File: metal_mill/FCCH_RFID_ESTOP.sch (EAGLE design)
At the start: 31 parts, among them Q1 BC846ALT1SMD, Q2 BC846ALT1SMD, Q3 2N3906, Q4 2N3906, Q5 2N3906

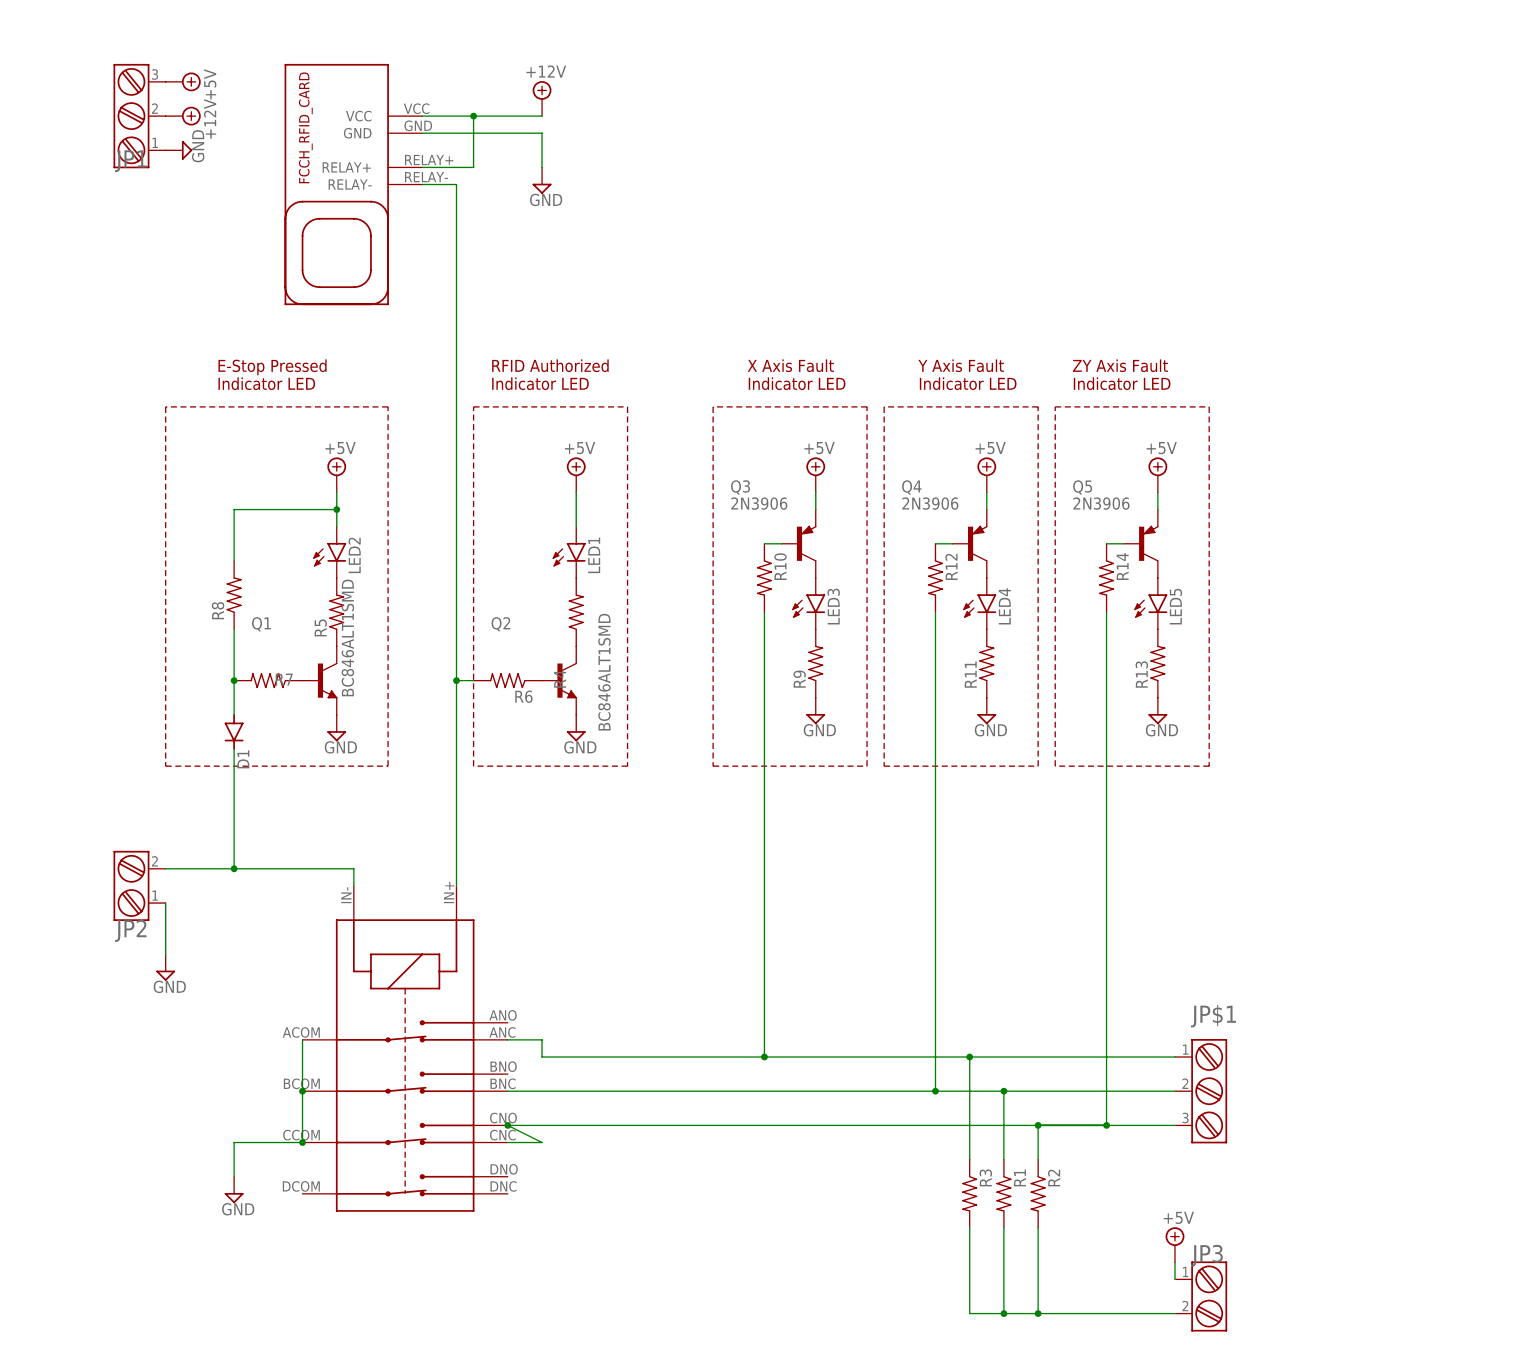
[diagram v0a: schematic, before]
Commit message: Added FCCH_RFID_ESTOP board layout and wire harnesses description in README.md
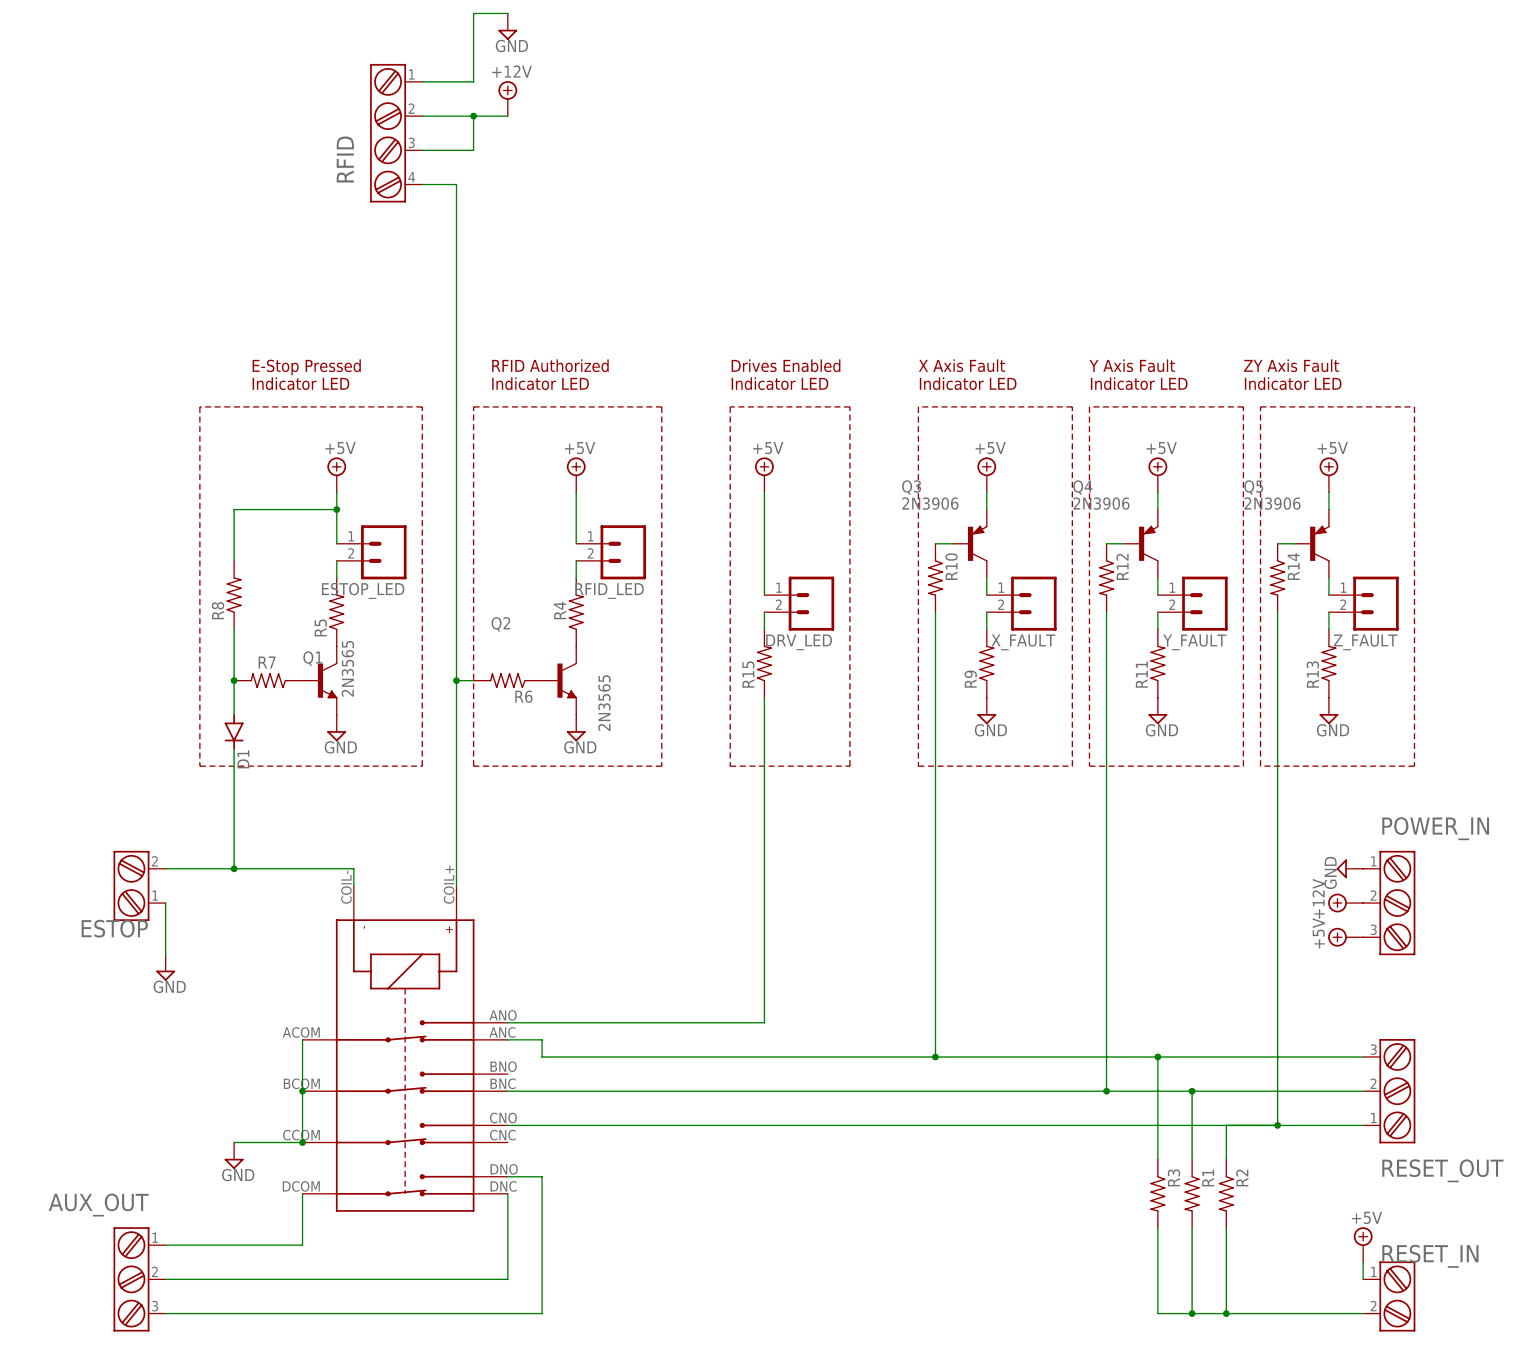
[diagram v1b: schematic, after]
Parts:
- removed JP$1, JP1: EURO-CON-3_2.54P, zahaComponents:EURO-CON-3_2.54P
- removed JP2, JP3: EURO-CON-2_2.54P, zahaComponents:EURO-CON-2_2.54P
- removed LED1, LED2, LED3, LED4, LED5: (no value), led:LED3MM
- removed U$2: RELAY_4PDT, fcch_eagle_parts_metal_mill:RELAY_4PDT
- removed U$3: FCCH_RFID_CARD, fcch_eagle_parts_metal_mill:FCCH_RFID_CARD
- added AUX_OUT, POWER_IN, RESET_OUT: EURO-CON-3_2.54P, fcch_eagle_parts_metal_mill:EURO-CON-3_2.54P
- added DRV_LED, ESTOP_LED, RFID_LED, X_FAULT, Y_FAULT, Z_FAULT: (no value), con-amp-quick:M02
- added ESTOP, RESET_IN: EURO-CON-2_2.54P, fcch_eagle_parts_metal_mill:EURO-CON-2_2.54P
- added R15: (no value), rcl:R-US_0204/7
- added RFID: EURO-CON-4_2.54P, fcch_eagle_parts_metal_mill:EURO-CON-4_2.54P
- added U$1: NC4D-JP-DC5V, fcch_eagle_parts_metal_mill:NC4D-JP-DC5V
- Q1, Q2: value BC846ALT1SMD -> 2N3565; device transistor-npn:BC846ALT1SMD -> transistor-npn:2N3565
- R1, R10, R11, R12, R13, R14, R2, R3, R4, R5, R6, R7, R8, R9: device rcl:R-US_M0805 -> rcl:R-US_0204/7
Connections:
- removed net N$1: JP$1.1, R10.2, R3.1, U$2.ANC
- removed net N$12: LED2.C, R5.2
- removed net N$13: D1.C, JP2.2, U$2.P$2
- removed net N$14: LED3.A, Q3.C
- removed net N$2: JP$1.2, R1.1, R12.2, U$2.BNC
- removed net N$3: JP$1.3, R14.2, R2.1, U$2.CNC, U$2.CNO
- removed net N$4: LED1.C, R4.2
- removed net N$6: R6.2, U$2.P$1, U$3.RELAY-
- new net ANO: R15.1, U$1.ANO
- new net AUX_RELAY_COM: AUX_OUT.1, U$1.DCOM
- new net AUX_RELAY_NC: AUX_OUT.2, U$1.DNC
- new net AUX_RELAY_NO: AUX_OUT.3, U$1.DNO
- new net ESTOP: D1.C, ESTOP.2, U$1.COIL-
- new net N$21: R9.2, X_FAULT.2
- new net N$25: R11.2, Y_FAULT.2
- new net N$26: Q5.C, Z_FAULT.1
- new net N$27: R13.2, Z_FAULT.2
- new net RFID_ENABLE: R6.2, RFID.4, U$1.COIL+
- new net X_ERR/RES: R10.2, R3.1, RESET_OUT.3, U$1.ANC
- new net Y_ERR/RES: R1.1, R12.2, RESET_OUT.2, U$1.BNC
- new net Z_ERR/RES: R14.2, R2.1, RESET_OUT.1, U$1.CNO
- net +12V: now also POWER_IN.2, RFID.2, RFID.3; no longer JP1.2, U$3.RELAY+, U$3.VCC
- net +5V: now also DRV_LED.1, ESTOP_LED.1, POWER_IN.3, RESET_IN.1, RFID_LED.1; no longer JP1.3, JP3.1, LED1.A, LED2.A
- net GND: now also ESTOP.1, POWER_IN.1, RFID.1, U$1.ACOM, U$1.BCOM, U$1.CCOM; no longer JP1.1, JP2.1, U$2.ACOM, U$2.BCOM, U$2.CCOM, U$3.GND
- net N$15: now also ESTOP_LED.2, R5.2; no longer LED3.C, R9.2
- net N$17: now also R4.2, RFID_LED.2; no longer LED4.A, Q4.C
- net N$18: now also DRV_LED.2, R15.2; no longer LED5.A, Q5.C
- net N$19: now also Q3.C, X_FAULT.1; no longer LED4.C, R11.2
- net N$23: now also Q4.C, Y_FAULT.1; no longer LED5.C, R13.2
- net N$7: now also RESET_IN.2; no longer JP3.2
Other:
- note added: "Drives Enabled Indicator LED"
- moved on the sheet: Q3, Q4, Q5, R1, R10, R11, R12, R13, R14, R2, R3, R9

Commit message: check point: before changing the reset relay to allow +5V as well as ground
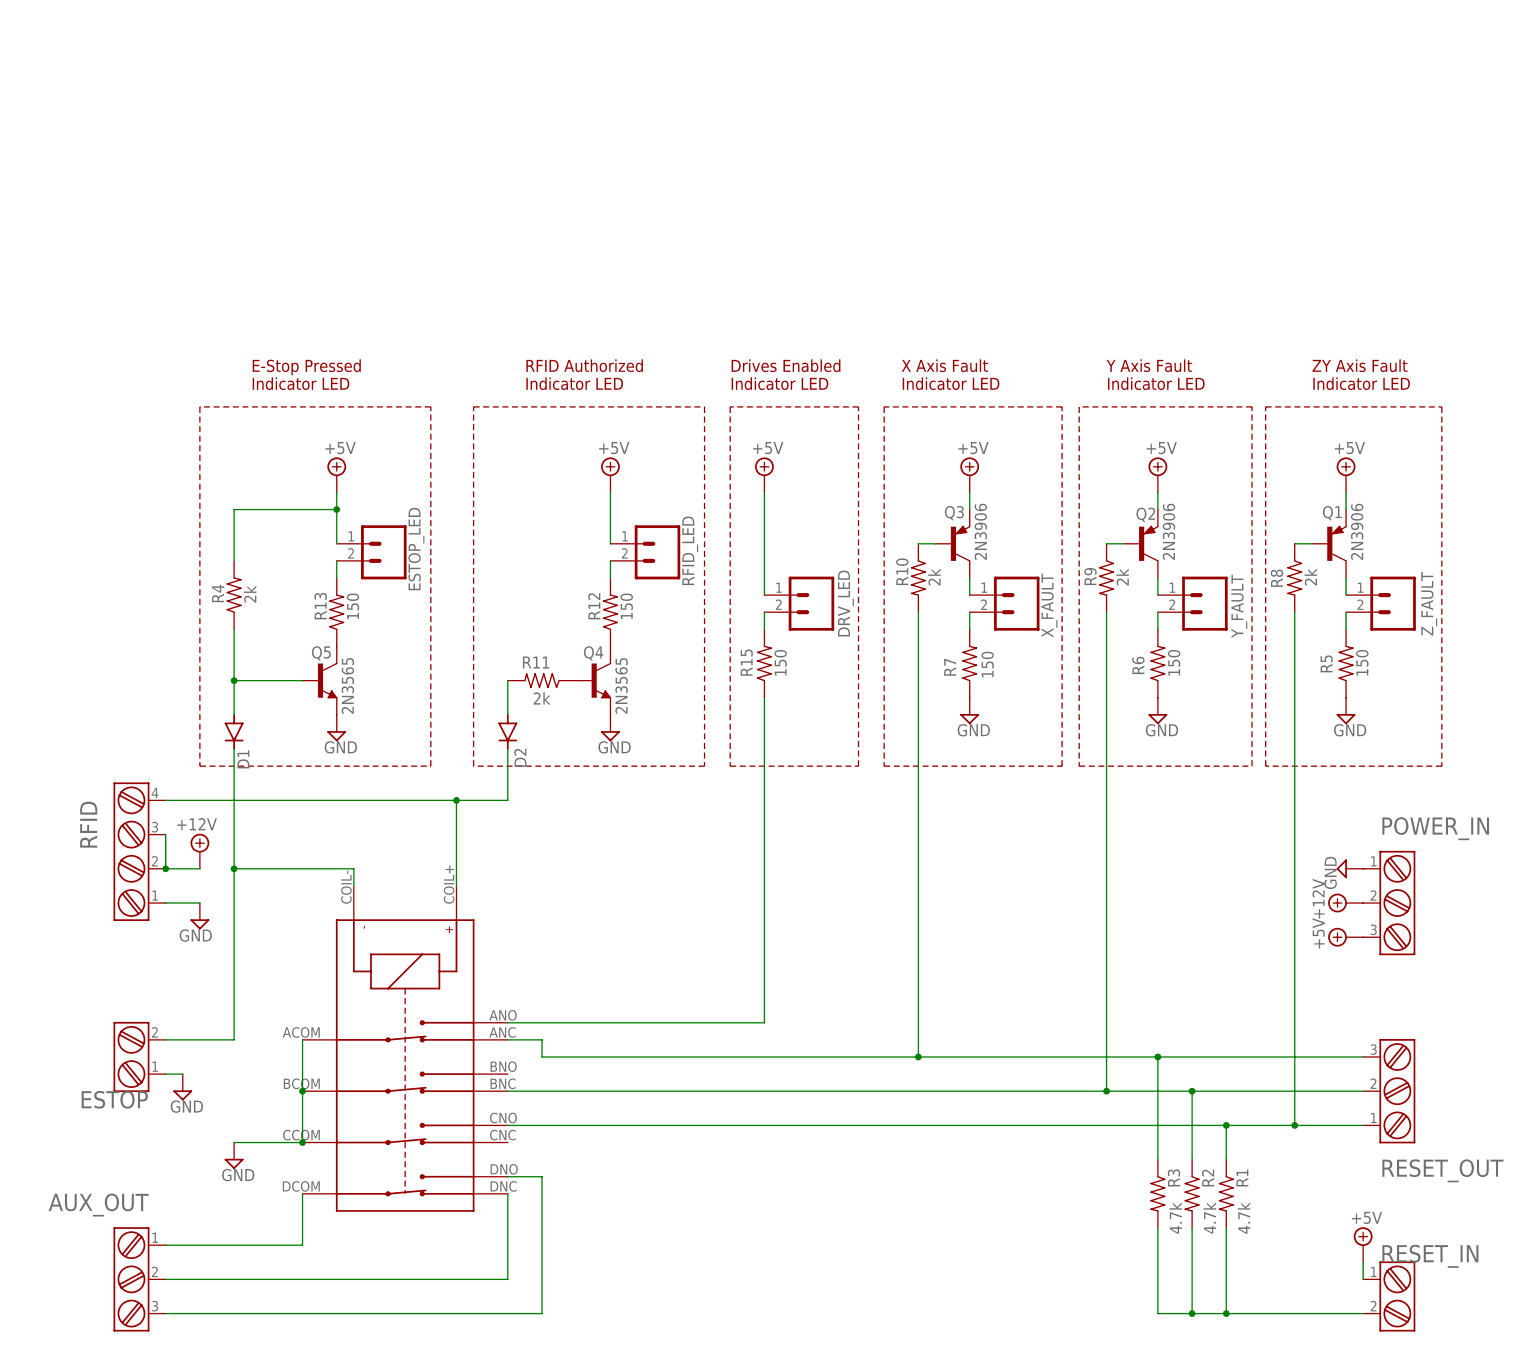
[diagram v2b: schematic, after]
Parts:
- removed R14: (no value), rcl:R-US_0204/7
- added D2: (no value), diode:DIODE-D-5
- Q1, Q2: value 2N3565 -> 2N3906; device transistor-npn:2N3565 -> transistor-pnp:2N3906
- Q4, Q5: value 2N3906 -> 2N3565; device transistor-pnp:2N3906 -> transistor-npn:2N3565
- R1, R2, R3: value (none) -> 4.7k
- R10, R11, R4, R8, R9: value (none) -> 2k
- R12, R13, R15, R5, R6, R7: value (none) -> 150
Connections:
- removed net N$10: Q1.B, R7.1
- new net N$1: D2.A, R11.2
- net +5V: now also Q1.E, Q2.E, R4.2; no longer Q4.E, Q5.E, R8.2
- net GND: now also Q4.E, Q5.E, R5.1, R6.1, R7.1; no longer Q1.E, Q2.E, R11.1, R13.1, R9.1
- net N$11: now also Q4.C, R12.1; no longer Q2.C, R4.1
- net N$15: now also R13.2; no longer R5.2
- net N$17: now also R12.2; no longer R4.2
- net N$20: now also Q2.B, R9.1; no longer Q4.B, R12.1
- net N$21: now also R7.2; no longer R9.2
- net N$23: now also Q2.C; no longer Q4.C
- net N$24: now also Q1.B, R8.1; no longer Q5.B, R14.1
- net N$25: now also R6.2; no longer R11.2
- net N$26: now also Q1.C; no longer Q5.C
- net N$27: now also R5.2; no longer R13.2
- net N$5: now also Q5.B, R4.1; no longer R7.2, R8.1
- net N$8: now also Q5.C, R13.1; no longer Q1.C, R5.1
- net N$9: now also Q4.B, R11.1; no longer Q2.B, R6.1
- net RFID_ENABLE: now also D2.C; no longer R6.2
- net Y_ERR/RES: now also R2.1, R9.2; no longer R1.1, R12.2
- net Z_ERR/RES: now also R1.1, R8.2; no longer R14.2, R2.1
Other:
- moved on the sheet: ESTOP, Q3, R1, R10, R11, R12, R13, R2, R4, R5, R6, R7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

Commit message: * changed reset_in to use the NO contacts of the relay * grouped the screw terminals that will connect to the GX16-8
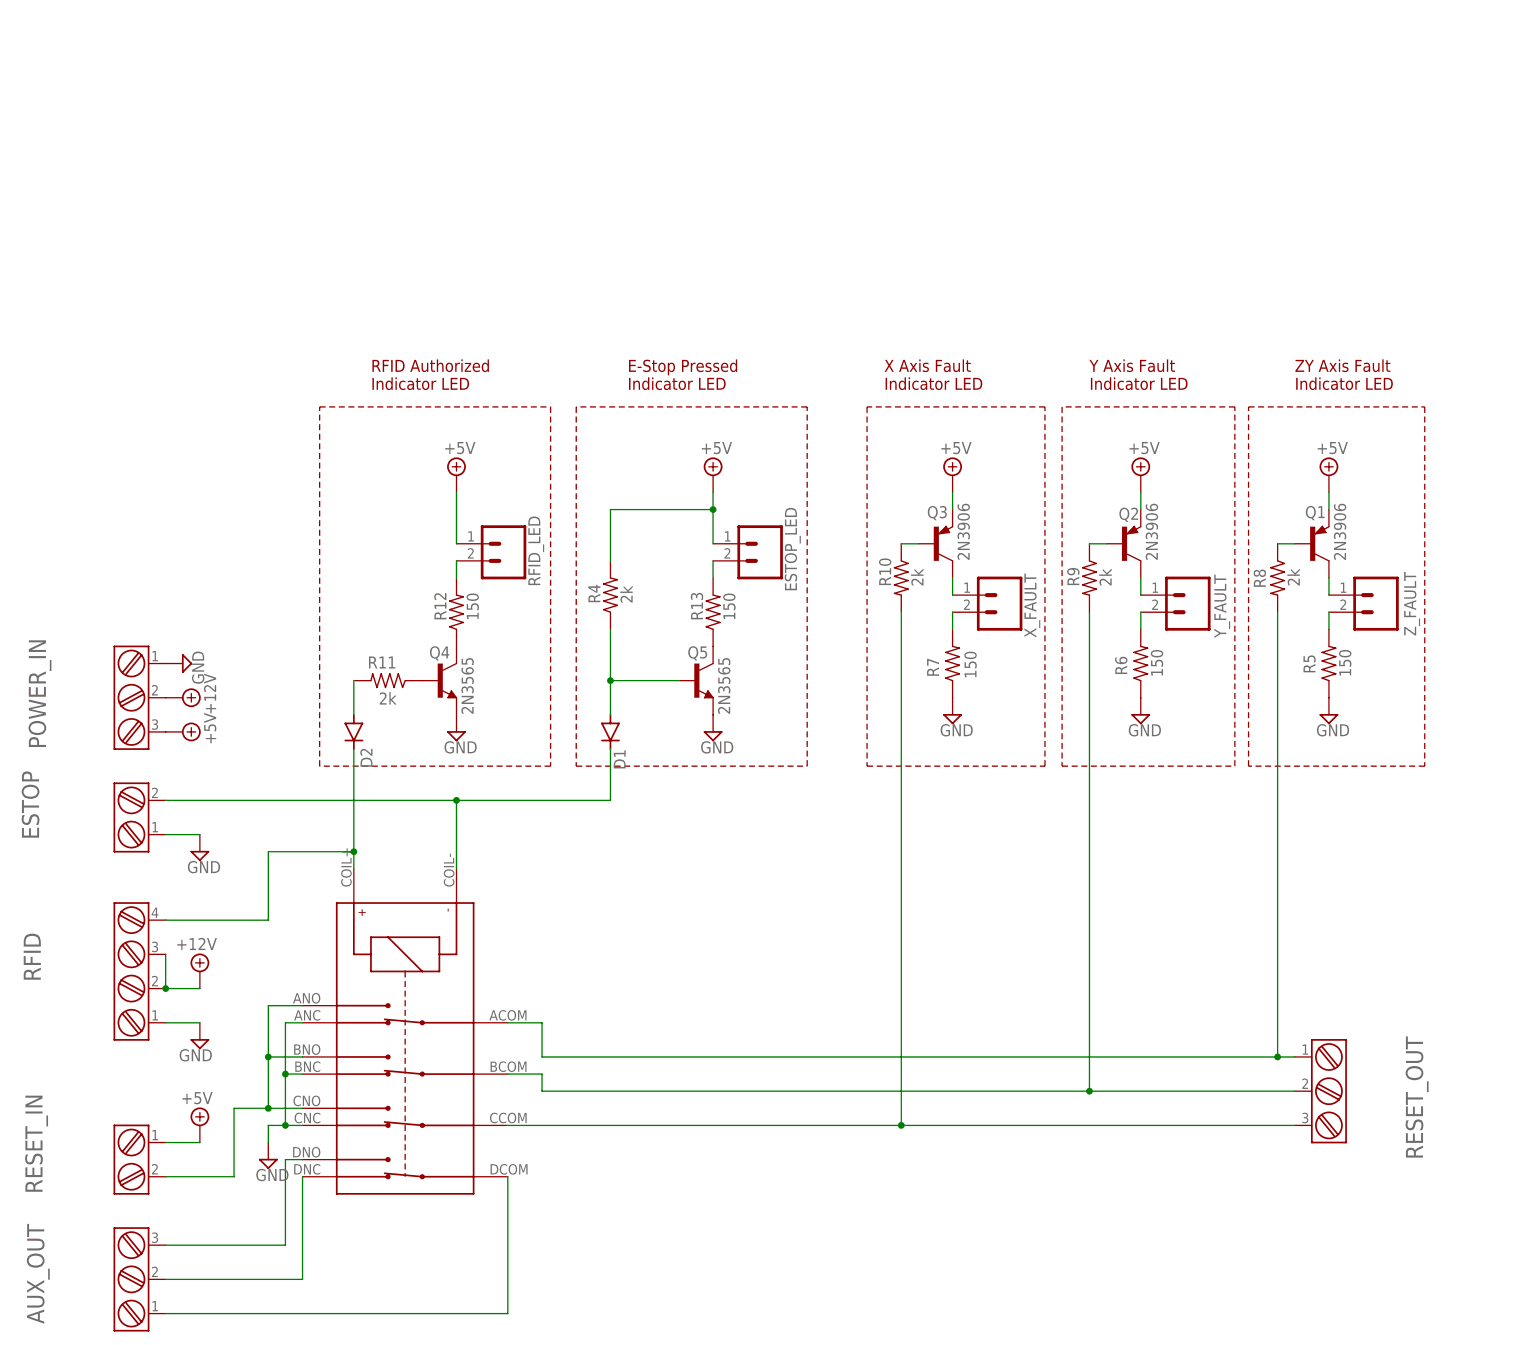
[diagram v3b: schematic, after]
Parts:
- removed DRV_LED: (no value), con-amp-quick:M02
- removed R1, R2, R3: 4.7k, rcl:R-US_0204/7
- removed R15: 150, rcl:R-US_0204/7
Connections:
- removed net ANO: R15.1, U$1.ANO
- removed net N$18: DRV_LED.2, R15.2
- removed net N$7: R1.2, R2.2, R3.2, RESET_IN.2
- new net N$2: RESET_IN.2, U$1.ANO, U$1.BNO, U$1.CNO
- net +5V: no longer DRV_LED.1
- net GND: now also U$1.ANC, U$1.BNC, U$1.CNC; no longer U$1.ACOM, U$1.BCOM, U$1.CCOM
- net X_ERR/RES: now also U$1.CCOM; no longer R3.1, U$1.ANC
- net Y_ERR/RES: now also U$1.BCOM; no longer R2.1, U$1.BNC
- net Z_ERR/RES: now also U$1.ACOM; no longer R1.1, U$1.CNO
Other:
- note removed: "Drives Enabled Indicator LED"
- moved on the sheet: AUX_OUT, D1, D2, ESTOP, ESTOP_LED, POWER_IN, Q1, Q2, Q3, Q4, Q5, R10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
